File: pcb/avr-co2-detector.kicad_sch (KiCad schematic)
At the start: 33 parts

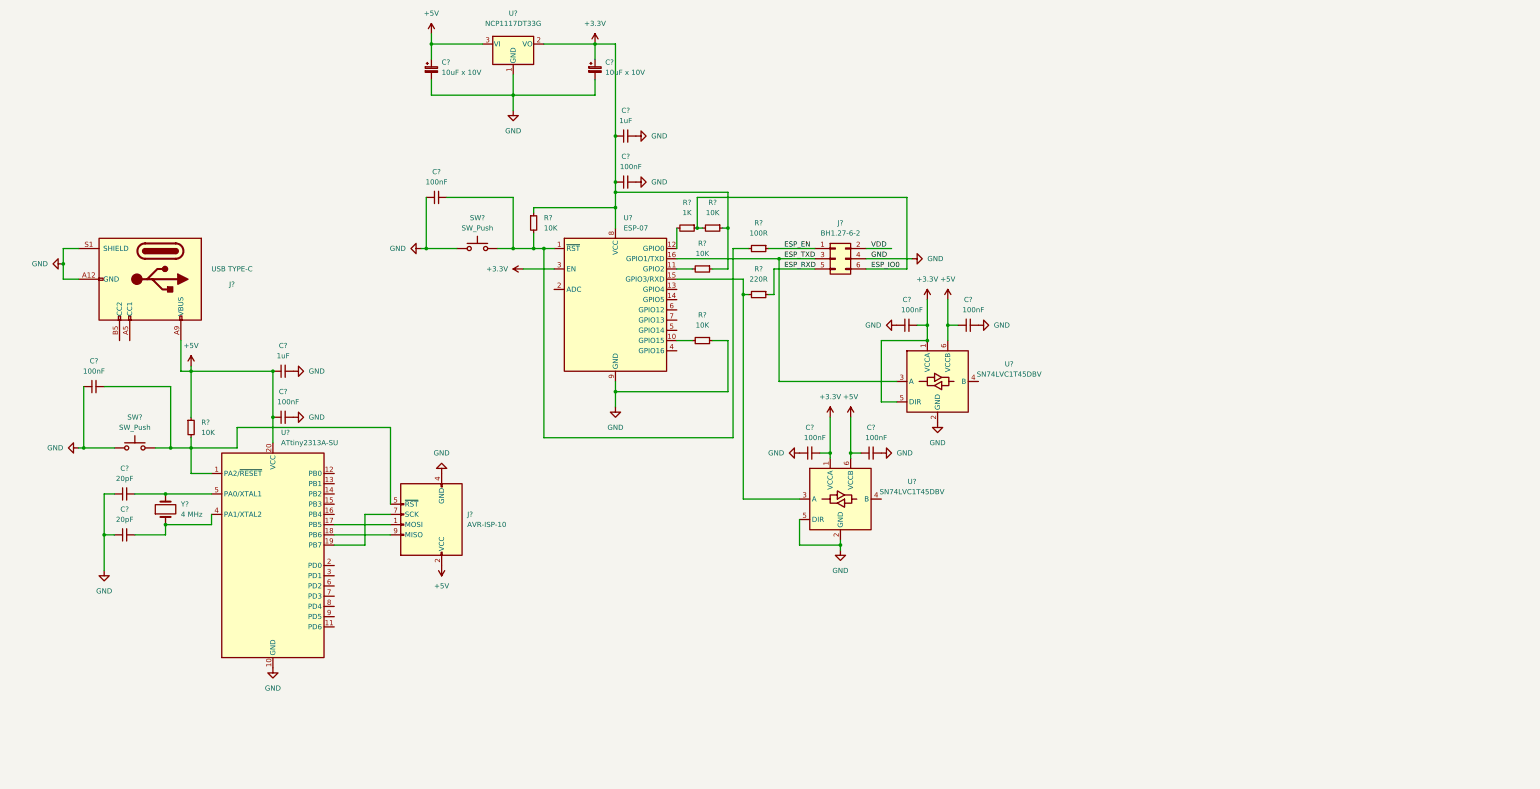
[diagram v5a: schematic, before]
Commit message: Added connector for LCD
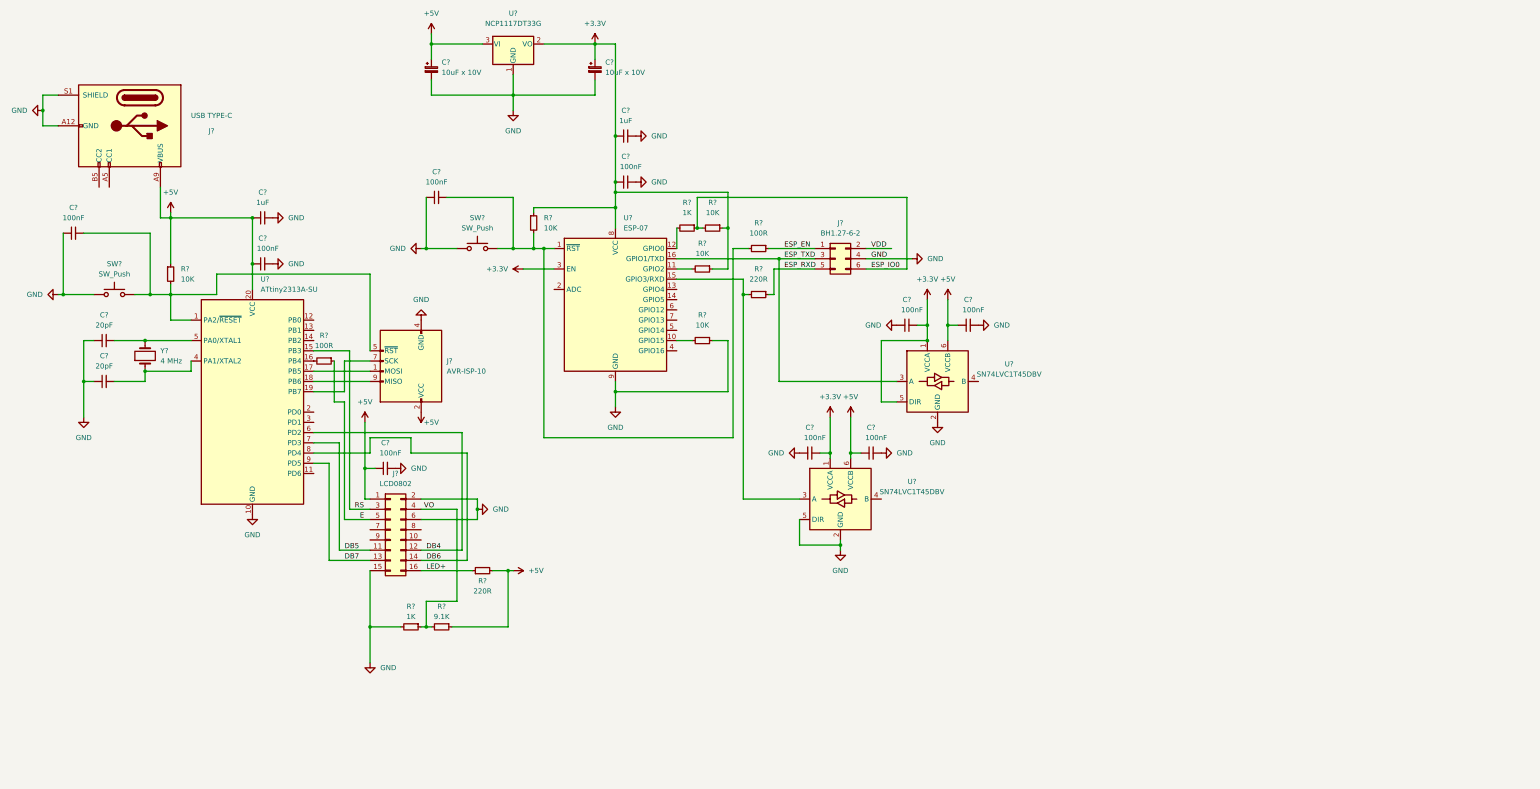
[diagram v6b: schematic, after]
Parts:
- added C?: 100nF, symbol Device:C_Small
- added J?: LCD0802, symbol Connector_Generic:Conn_02x08_Odd_Even
- added R?: 100R, symbol Device:R_Small
- added R?: 220R, symbol Device:R_Small
- added R?: 9.1K, symbol Device:R_Small
- added R?: 1K, symbol Device:R_Small
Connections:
- net +5V: now also C?.1, J?.1 (Pin_1), R?.1, R?.2
- net GND: now also C?.2, J?.15 (Pin_15), J?.2 (Pin_2), J?.6 (Pin_6), R?.2
- net RS: now reaches U?.15 (PB3)
- net RS: now also J?.3 (Pin_3)
- net at U?.16 (PB4): now also R?.2
- net DB4: now reaches U?.6 (PD2)
- net DB4: now also J?.12 (Pin_12)
- net DB5: now reaches U?.7 (PD3)
- net DB5: now also J?.11 (Pin_11)
- net DB6: now reaches U?.8 (PD4)
- net DB6: now also J?.14 (Pin_14)
- net DB7: now reaches U?.9 (PD5)
- net DB7: now also J?.13 (Pin_13)
- new net E: J?.5 (Pin_5), R?.1
- new net LED+: J?.16 (Pin_16), R?.1
- new net VO: J?.4 (Pin_4), R?.1, R?.2
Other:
- moved on the sheet: C?, J?, R?, SW?, U?, Y?

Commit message: Changed symbol Connector:USB_C_Receptacle_PowerOnly_6P to Connector:USB_C_Receptacle_USB2.0
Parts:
- removed J?: USB TYPE-C, Connector_USB:USB_C_Receptacle_HRO_TYPE-C-31-M-12, symbol Connector:USB_C_Receptacle_PowerOnly_6P
- added J?: USB TYPE-C, Connector_USB:USB_C_Receptacle_HRO_TYPE-C-31-M-12, symbol Connector:USB_C_Receptacle_USB2.0
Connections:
- net +5V: now also J?.A4 (VBUS), J?.A9 (VBUS), J?.B4 (VBUS), J?.B9 (VBUS)
- net GND: now also J?.A1 (GND), J?.A12 (GND), J?.B1 (GND), J?.B12 (GND), J?.S1 (SHIELD)
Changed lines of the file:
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@@
   (junction (at 55.88 68.58) (diameter 0) (color 0 0 0 0)
   )
+  (junction (at 30.48 34.29) (diameter 0) (color 0 0 0 0)
+  )
   (junction (at 224.79 127) (diameter 0) (color 0 0 0 0)
   )
@@
   (junction (at 219.71 127) (diameter 0) (color 0 0 0 0)
   )
-  (junction (at 24.13 41.91) (diameter 0) (color 0 0 0 0)
-  )
   (junction (at 166.37 48.26) (diameter 0) (color 0 0 0 0)
   )
@@
     (stroke (width 0) (type default) (color 0 0 0 0))
   )
-  (wire (pts (xy 24.13 38.1) (xy 24.13 41.91))
-    (stroke (width 0) (type default) (color 0 0 0 0))
-  )
   (wire (pts (xy 243.84 95.25) (xy 243.84 99.06))
     (stroke (width 0) (type default) (color 0 0 0 0))
@@
     (stroke (width 0) (type default) (color 0 0 0 0))
   )
-  (wire (pts (xy 27.94 38.1) (xy 24.13 38.1))
-    (stroke (width 0) (type default) (color 0 0 0 0))
-  )
   (wire (pts (xy 207.01 109.22) (xy 207.01 78.74))
     (stroke (width 0) (type default) (color 0 0 0 0))
@@
     (stroke (width 0) (type default) (color 0 0 0 0))
   )
+  (wire (pts (xy 30.48 30.48) (xy 30.48 34.29))
+    (stroke (width 0) (type default) (color 0 0 0 0))
+  )
   (wire (pts (xy 49.53 99.06) (xy 60.96 99.06))
     (stroke (width 0) (type default) (color 0 0 0 0))
@@
     (stroke (width 0) (type default) (color 0 0 0 0))
   )
-  (wire (pts (xy 27.94 45.72) (xy 24.13 45.72))
-    (stroke (width 0) (type default) (color 0 0 0 0))
-  )
   (wire (pts (xy 34.29 99.06) (xy 34.29 109.22))
     (stroke (width 0) (type default) (color 0 0 0 0))
@@
     (stroke (width 0) (type default) (color 0 0 0 0))
   )
+  (wire (pts (xy 53.34 60.96) (xy 68.58 60.96))
+    (stroke (width 0) (type default) (color 0 0 0 0))
+  )
+  (wire (pts (xy 30.48 38.1) (xy 30.48 34.29))
+    (stroke (width 0) (type default) (color 0 0 0 0))
+  )
   (wire (pts (xy 222.25 151.13) (xy 222.25 149.86))
     (stroke (width 0) (type default) (color 0 0 0 0))
@@
     (stroke (width 0) (type default) (color 0 0 0 0))
   )
+  (wire (pts (xy 68.58 60.96) (xy 68.58 53.34))
+    (stroke (width 0) (type default) (color 0 0 0 0))
+  )
   (wire (pts (xy 99.06 104.14) (xy 105.41 104.14))
     (stroke (width 0) (type default) (color 0 0 0 0))
@@
   )
   (wire (pts (xy 95.25 129.54) (xy 91.44 129.54))
-    (stroke (width 0) (type default) (color 0 0 0 0))
-  )
-  (wire (pts (xy 24.13 45.72) (xy 24.13 41.91))
     (stroke (width 0) (type default) (color 0 0 0 0))
   )
@@
     (pin "1")
     (pin "2")
-  )
-  (symbol (lib_id "power:GND") (at 24.13 41.91 270) (unit 1)
-    (in_bom yes) (on_board yes) (fields_autoplaced)
-    (property "Reference" "#PWR?" (id 0) (at 17.78 41.91 0)
-      (effects (font (size 1.27 1.27)) hide)
-    )
-    (property "Value" "GND" (id 1) (at 20.32 41.9099 90)
-      (effects (font (size 1.27 1.27)) (justify right))
-    )
-    (property "Footprint" "" (id 2) (at 24.13 41.91 0)
-      (effects (font (size 1.27 1.27)) hide)
-    )
-    (property "Datasheet" "" (id 3) (at 24.13 41.91 0)
-      (effects (font (size 1.27 1.27)) hide)
-    )
-    (pin "1")
   )
   (symbol (lib_id "power:+3.3V") (at 219.71 118.11 0) (unit 1)
@@
     (pin "1")
   )
-  (symbol (lib_id "Connector:USB_C_Receptacle_PowerOnly_6P") (at 45.72 45.72 270) (unit 1)
-    (in_bom yes) (on_board yes)
-    (property "Reference" "J?" (id 0) (at 66.04 46.99 90))
-    (property "Value" "USB TYPE-C" (id 1) (at 66.04 43.18 90))
-    (property "Footprint" "Connector_USB:USB_C_Receptacle_HRO_TYPE-C-31-M-12" (id 2) (at 48.26 49.53 0)
-      (effects (font (size 1.27 1.27)) hide)
-    )
-    (property "Datasheet" "https://www.usb.org/sites/default/files/documents/usb_type-c.zip" (id 3) (at 45.72 45.72 0)
-      (effects (font (size 1.27 1.27)) hide)
-    )
-    (pin "A12")
-    (pin "A5")
-    (pin "A9")
-    (pin "B12")
-    (pin "B5")
-    (pin "B9")
-    (pin "S1")
-  )
   (symbol (lib_id "power:GND") (at 212.09 127 270) (unit 1)
     (in_bom yes) (on_board yes) (fields_autoplaced)
@@
     )
     (property "Datasheet" "" (id 3) (at 55.88 67.31 0)
+      (effects (font (size 1.27 1.27)) hide)
+    )
+    (pin "1")
+  )
+  (symbol (lib_id "power:GND") (at 30.48 34.29 270) (unit 1)
+    (in_bom yes) (on_board yes) (fields_autoplaced)
+    (property "Reference" "#PWR?" (id 0) (at 24.13 34.29 0)
+      (effects (font (size 1.27 1.27)) hide)
+    )
+    (property "Value" "GND" (id 1) (at 26.67 34.2899 90)
+      (effects (font (size 1.27 1.27)) (justify right))
+    )
+    (property "Footprint" "" (id 2) (at 30.48 34.29 0)
+      (effects (font (size 1.27 1.27)) hide)
+    )
+    (property "Datasheet" "" (id 3) (at 30.48 34.29 0)
       (effects (font (size 1.27 1.27)) hide)
     )
@@
     (pin "1")
   )
+  (symbol (lib_id "Connector:USB_C_Receptacle_USB2.0") (at 53.34 38.1 270) (unit 1)
+    (in_bom yes) (on_board yes) (fields_autoplaced)
+    (property "Reference" "J?" (id 0) (at 72.39 36.8299 90)
+      (effects (font (size 1.27 1.27)) (justify left))
+    )
+    (property "Value" "USB TYPE-C" (id 1) (at 72.39 39.3699 90)
+      (effects (font (size 1.27 1.27)) (justify left))
+    )
+    (property "Footprint" "Connector_USB:USB_C_Receptacle_HRO_TYPE-C-31-M-12" (id 2) (at 53.34 41.91 0)
+      (effects (font (size 1.27 1.27)) hide)
+    )
+    (property "Datasheet" "https://www.usb.org/sites/default/files/documents/usb_type-c.zip" (id 3) (at 53.34 41.91 0)
+      (effects (font (size 1.27 1.27)) hide)
+    )
+    (pin "A1")
+    (pin "A12")
+    (pin "A4")
+    (pin "A5")
+    (pin "A6")
+    (pin "A7")
+    (pin "A8")
+    (pin "A9")
+    (pin "B1")
+    (pin "B12")
+    (pin "B4")
+    (pin "B5")
+    (pin "B6")
+    (pin "B7")
+    (pin "B8")
+    (pin "B9")
+    (pin "S1")
+  )
   (symbol (lib_id "Device:C_Small") (at 168.91 59.69 90) (unit 1)
     (in_bom yes) (on_board yes)
@@
       (reference "#PWR?") (unit 1) (value "GND") (footprint "")
     )
-    (path "/41182ee8-78dc-45c9-8616-06bc53e6952c"
-      (reference "#PWR?") (unit 1) (value "GND") (footprint "")
-    )
     (path "/492186da-a762-4e0b-ba90-c09c7f3a3a03"
       (reference "#PWR?") (unit 1) (value "+3.3V") (footprint "")
@@
       (reference "#PWR?") (unit 1) (value "+5V") (footprint "")
     )
+    (path "/c50d8e9b-0b5f-4f71-95d2-04542aed80e7"
+      (reference "#PWR?") (unit 1) (value "GND") (footprint "")
+    )
     (path "/c5db6a54-9818-4823-8978-b12ba5ae3bf3"
       (reference "#PWR?") (unit 1) (value "GND") (footprint "")
@@
       (reference "J?") (unit 1) (value "LCD0802") (footprint "")
     )
-    (path "/56963627-a9df-4434-983c-b60a2bd5363c"
-      (reference "J?") (unit 1) (value "USB TYPE-C") (footprint "Connector_USB:USB_C_Receptacle_HRO_TYPE-C-31-M-12")
-    )
     (path "/7331dd53-b74c-407d-99f2-d04a0d92ca38"
       (reference "J?") (unit 1) (value "BH1.27-6-2") (footprint "")
@@
       (reference "J?") (unit 1) (value "AVR-ISP-10") (footprint "")
     )
+    (path "/fe24c7f9-f2f0-4563-baff-d0b51b8d917d"
+      (reference "J?") (unit 1) (value "USB TYPE-C") (footprint "Connector_USB:USB_C_Receptacle_HRO_TYPE-C-31-M-12")
+    )
     (path "/09a93844-90f2-469e-82e8-a867b25e01c2"

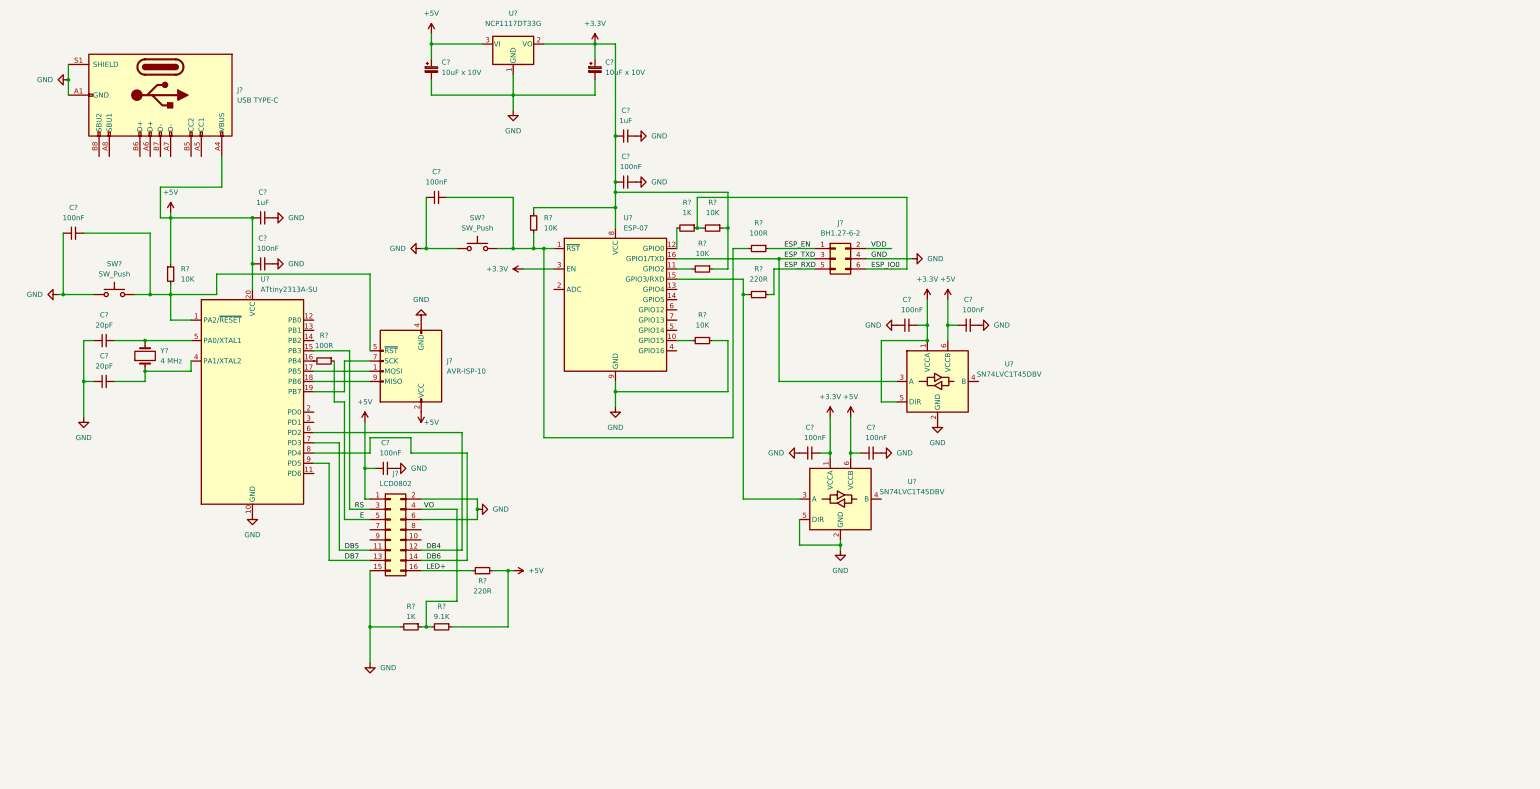
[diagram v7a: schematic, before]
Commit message: Added USB to serial UART interface for debugging ATtiny2313A
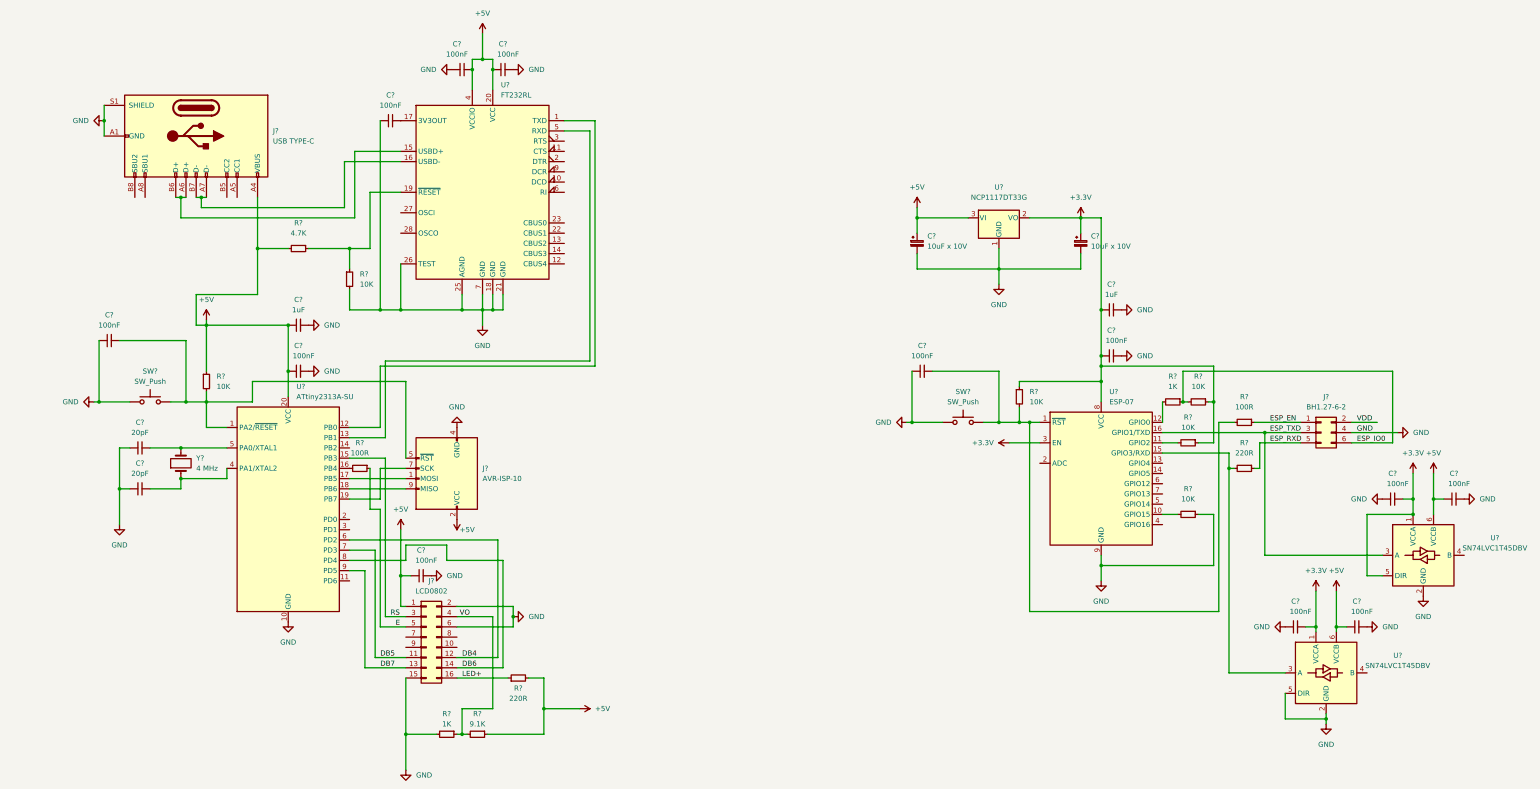
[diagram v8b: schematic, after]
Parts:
- added C? (x3): 100nF, symbol Device:C_Small
- added R?: 4.7K, symbol Device:R_Small
- added R?: 10K, symbol Device:R_Small
- added U?: FT232RL, Package_SO:SSOP-28_5.3x10.2mm_P0.65mm, symbol Interface_USB:FT232RL
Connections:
- net +5V: now also C?.1, C?.1, R?.2, U?.20 (VCC), U?.4 (VCCIO)
- net GND: now also C?.1, C?.2, C?.2, R?.2, U?.18 (GND), U?.21 (GND), U?.25 (AGND), U?.26 (TEST), U?.7 (GND)
- net at U?.12 (PB0): now also U?.1 (TXD)
- net at U?.13 (PB1): now also U?.5 (RXD)
- net at J?.A6 (D+): now also J?.B6 (D+), U?.15 (USBD+)
- net at J?.A7 (D-): now also J?.B7 (D-), U?.16 (USBD-)
- new net: C?.2, U?.17 (3V3OUT)
- new net: R?.1, R?.1, U?.19 (~{RESET})
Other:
- moved on the sheet: C?, J?, R?, SW?, U?, Y?
